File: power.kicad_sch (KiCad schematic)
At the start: 47 parts, among them J3 Barrel_Jack_Switch, Q10 RJK0355DSP, Q7 DMP3037LSS-13, Q8 2N7002, Q9 RJK0355DSP, U5 MIC2101

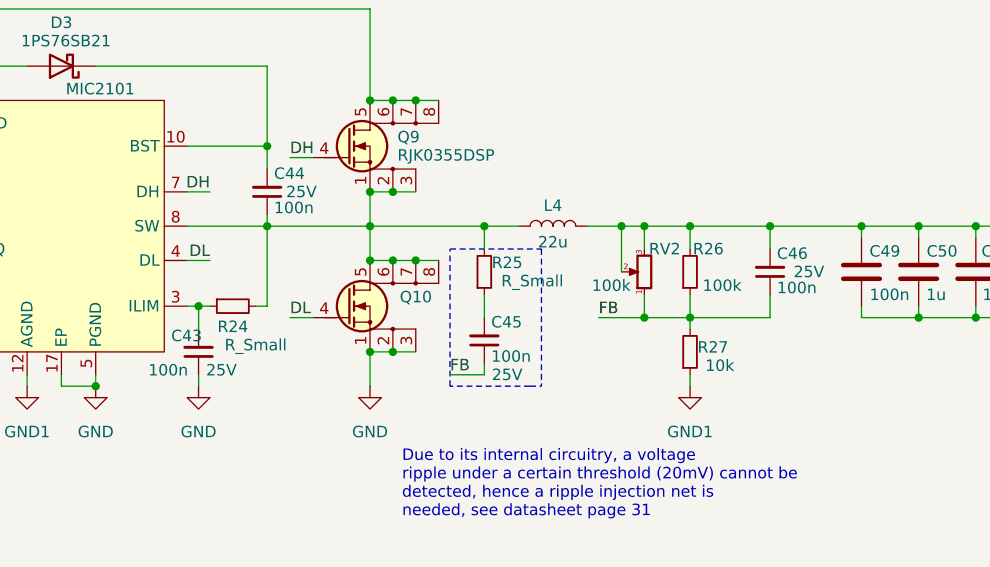
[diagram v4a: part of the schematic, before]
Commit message: small corrections to PCB, fixed some capacitors' voltage ratings and footprints to make BOM more uniform
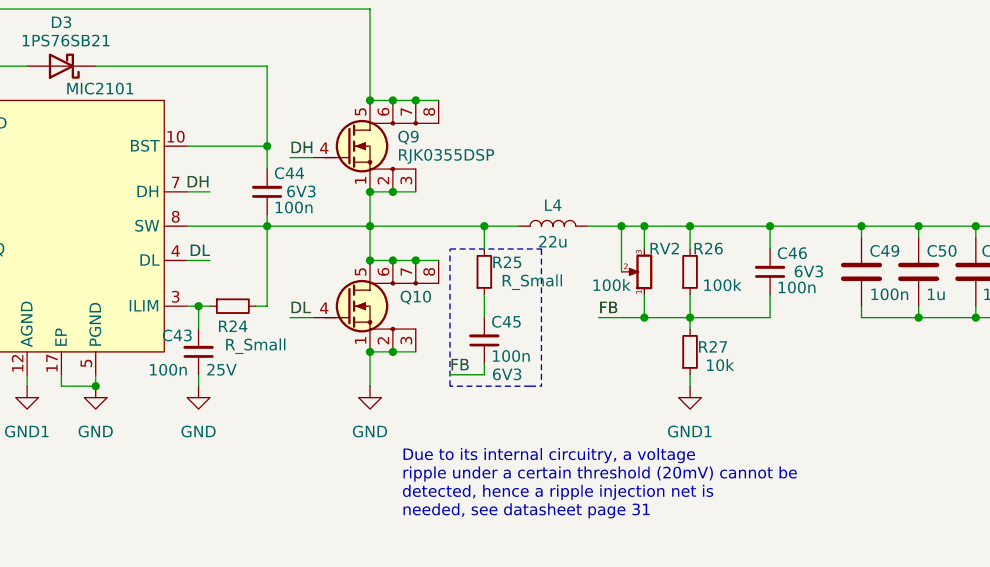
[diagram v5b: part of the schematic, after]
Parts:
- C41, C42: Voltage Rating 25V -> 16V
- C44, C45, C46: footprint Capacitor_SMD:C_0805_2012Metric -> Capacitor_SMD:C_0603_1608Metric; Voltage Rating 25V -> 6V3
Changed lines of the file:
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@@
 			)
 		)
-		(property "Footprint" "Capacitor_SMD:C_0805_2012Metric"
+		(property "Footprint" "Capacitor_SMD:C_0603_1608Metric"
 			(at 146.05 50.8 0)
 			(effects
@@
 			)
 		)
-		(property "Voltage Rating" "25V"
+		(property "Voltage Rating" "6V3"
 			(at 149.86 50.8 0)
 			(effects
@@
 			)
 		)
-		(property "Voltage Rating" "25V"
+		(property "Voltage Rating" "16V"
 			(at 104.14 39.37 0)
 			(effects
@@
 			)
 		)
-		(property "Voltage Rating" "25V"
+		(property "Voltage Rating" "16V"
 			(at 104.14 46.99 0)
 			(effects
@@
 			)
 		)
-		(property "Footprint" "Capacitor_SMD:C_0805_2012Metric"
+		(property "Footprint" "Capacitor_SMD:C_0603_1608Metric"
 			(at 170.18 67.31 0)
 			(effects
@@
 			)
 		)
-		(property "Voltage Rating" "25V"
+		(property "Voltage Rating" "6V3"
 			(at 172.72 71.12 0)
 			(effects
@@
 			)
 		)
+		(property "Store Link" ""
+			(at 170.18 67.31 0)
+			(effects
+				(font
+					(size 1.27 1.27)
+				)
+				(hide yes)
+			)
+		)
+		(property "Dielectric (capacitors)" ""
+			(at 170.18 67.31 0)
+			(effects
+				(font
+					(size 1.27 1.27)
+				)
+				(hide yes)
+			)
+		)
+		(property "PN" ""
+			(at 170.18 67.31 0)
+			(effects
+				(font
+					(size 1.27 1.27)
+				)
+				(hide yes)
+			)
+		)
 		(pin "1"
 		)
@@
 			)
 		)
-		(property "Footprint" "Capacitor_SMD:C_0805_2012Metric"
+		(property "Footprint" "Capacitor_SMD:C_0603_1608Metric"
 			(at 201.93 59.69 0)
 			(effects
@@
 			)
 		)
-		(property "Voltage Rating" "25V"
+		(property "Voltage Rating" "6V3"
 			(at 206.248 59.69 0)
 			(effects
@@
 			)
 		)
+		(property "Store Link" ""
+			(at 201.93 59.69 0)
+			(effects
+				(font
+					(size 1.27 1.27)
+				)
+				(hide yes)
+			)
+		)
+		(property "Dielectric (capacitors)" ""
+			(at 201.93 59.69 0)
+			(effects
+				(font
+					(size 1.27 1.27)
+				)
+				(hide yes)
+			)
+		)
+		(property "PN" ""
+			(at 201.93 59.69 0)
+			(effects
+				(font
+					(size 1.27 1.27)
+				)
+				(hide yes)
+			)
+		)
 		(pin "1"
 		)
@@
 		(dnp no)
 		(property "Reference" "C43"
-			(at 135.382 66.802 0)
+			(at 134.366 66.802 0)
 			(effects
 				(font

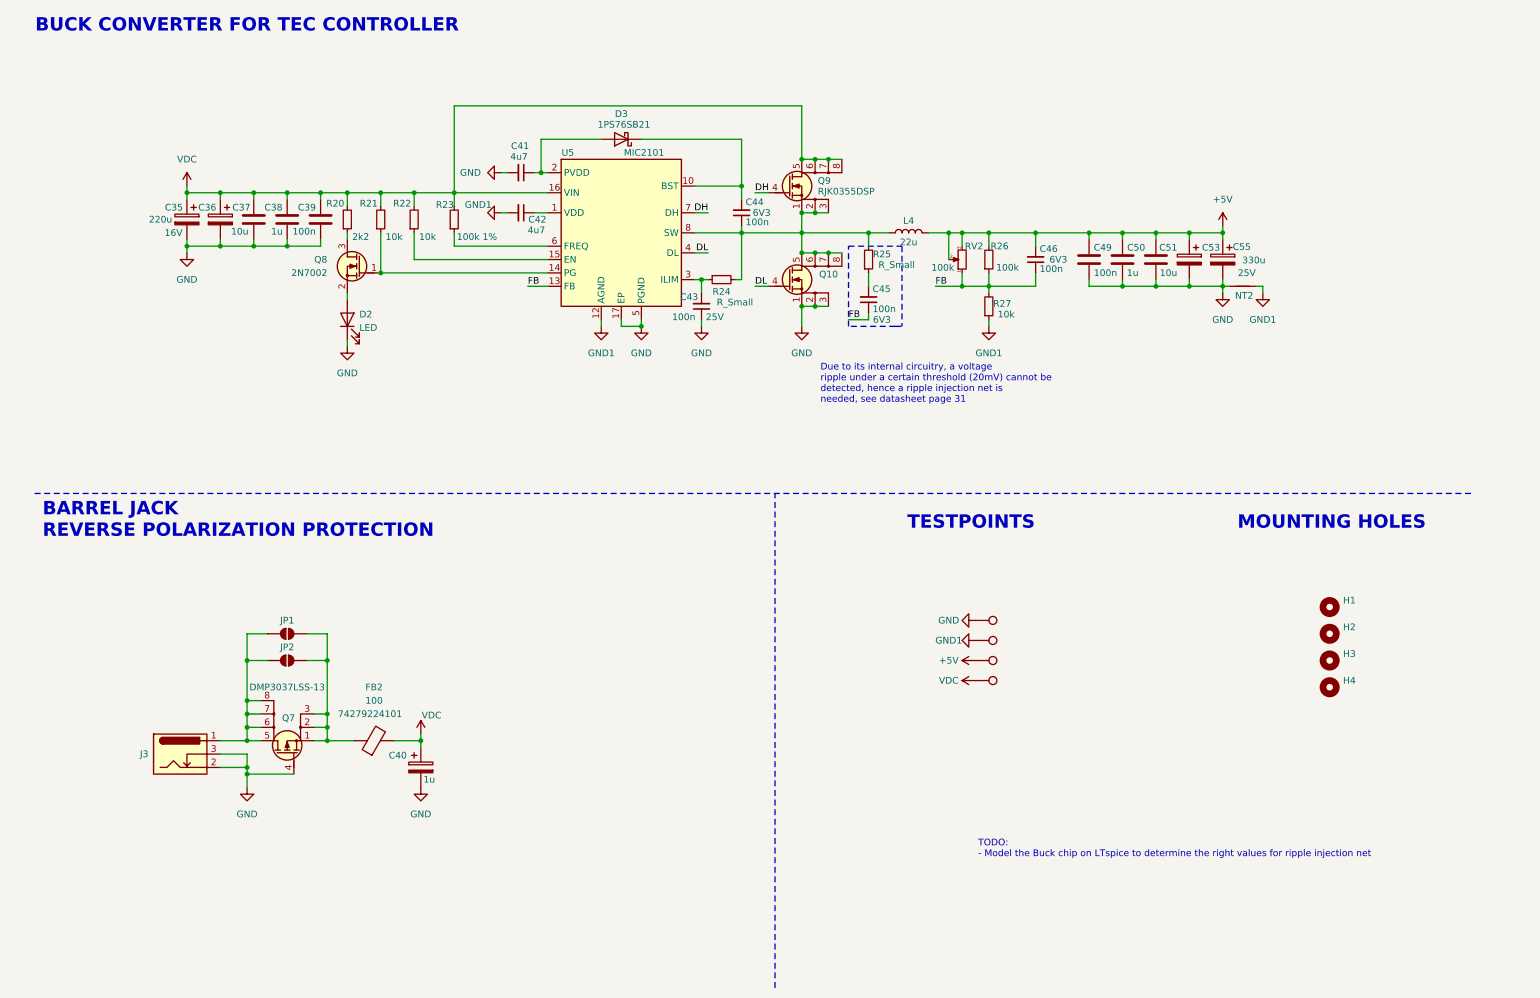
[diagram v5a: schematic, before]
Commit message: feat: made possible to swap butterfly pins for compatibility
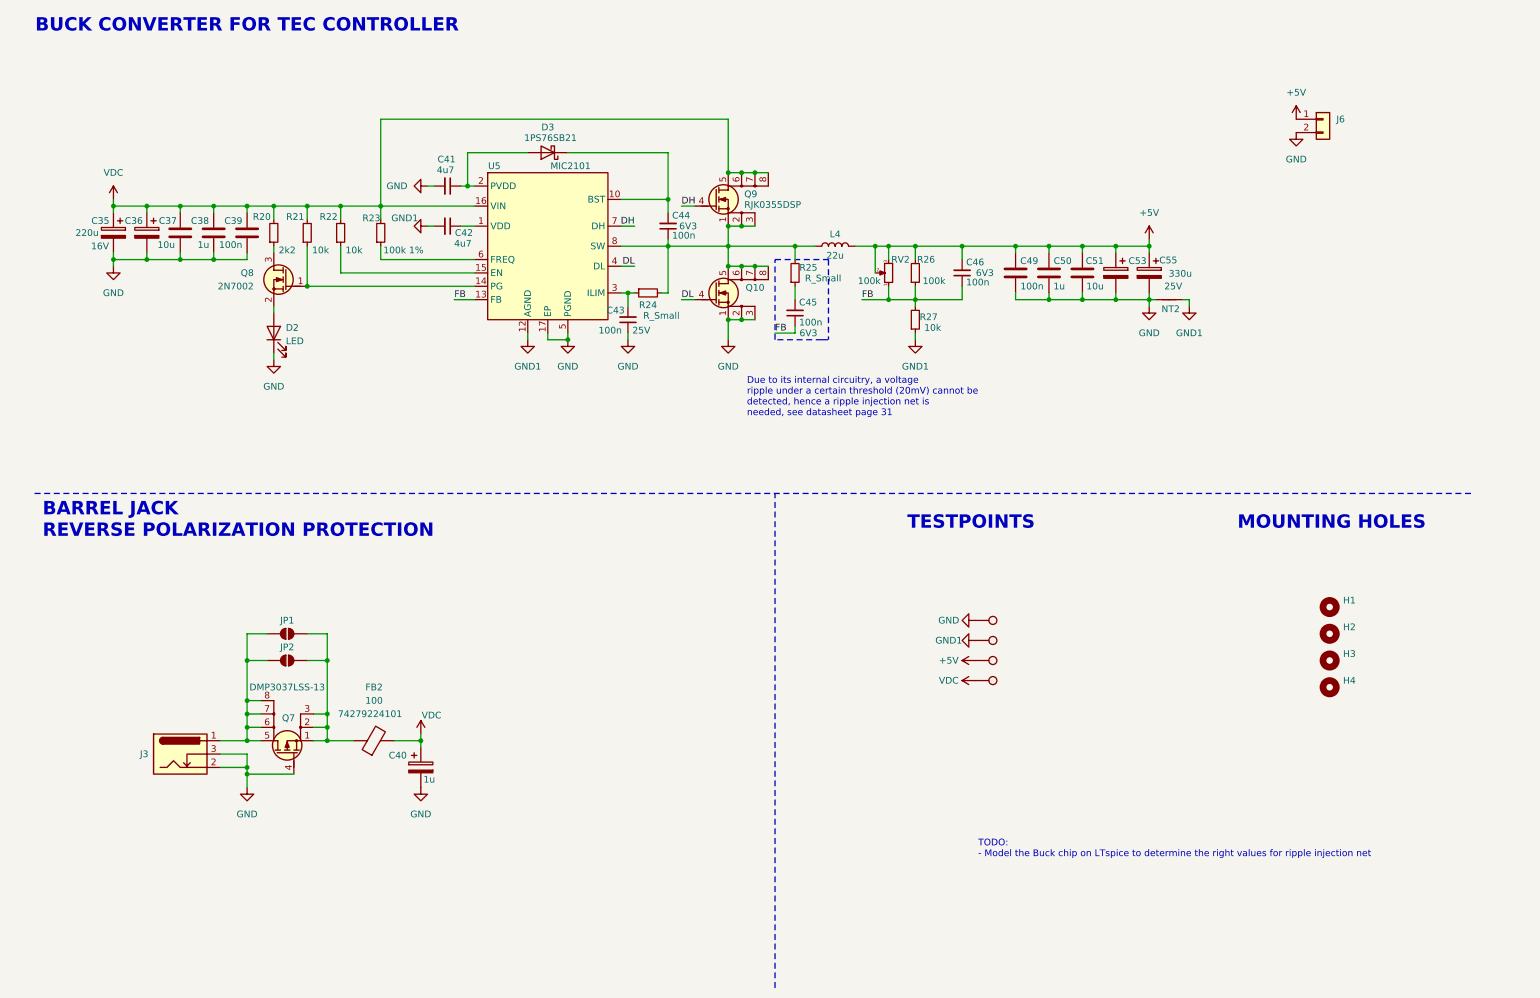
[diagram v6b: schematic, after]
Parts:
- added J6: Conn_01x02, Connector_JST:JST_XH_B2B-XH-AM_1x02_P2.50mm_Vertical, symbol Connector_Generic:Conn_01x02
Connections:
- net +5V: now also J6.1 (Pin_1)
- net GND: now also J6.2 (Pin_2)
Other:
- moved on the sheet: C35, C36, C37, C38, C39, C41, C42, C43, C44, C45, C46, C49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

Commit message: fix: small corrections to the pcb, added PNs and store link to mouser for each component
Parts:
- C35, C36: PN (none) -> EDK227M025A9MAA; Store Link (none) -> https://www.mouser.it/ProductDetail/KEMET/EDK227M025A9MAA?q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
- C37, C51: PN (none) -> TMK212BBJ106MG-T; Store Link (none) -> https://www.mouser.it/ProductDetail/TAIYO-YUDEN/TMK212BBJ10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
- C38, C50: PN (none) -> 885012207078; Store Link (none) -> https://www.mouser.it/ProductDetail/Wurth-Elektronik/885012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
- C39, C43, C49: PN (none) -> CL21F104ZBANNNC; Store Link (none) -> https://www.mouser.it/ProductDetail/Samsung-Electro-Mechani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
- C40: PN EEV337M025S9MAA -> EDH105M050A9BAA; Store Link (none) -> https://www.mouser.it/ProductDetail/KEMET/EDH105M050A9BAA?q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
- C41, C42: PN (none) -> C1608X5R1E475K080AC; Store Link (none) -> https://www.mouser.it/ProductDetail/TDK/C1608X5R1E475K080AC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
- C44, C46: PN (none) -> CL10B104KB8NNND; Store Link (none) -> https://www.mouser.it/ProductDetail/Samsung-Electro-Mechani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
- C45: PN (none) -> CL10B104KB8NNND; Store Link (none) -> https://www.mouser.it/ProductDetail/Samsung-Electro-Mechani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; now left out of the parts list
- C53, C55: Store Link (none) -> https://www.mouser.it/ProductDetail/KEMET/EEV337M025S9MAA?q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
- D2, R24, R25, TP12, TP13, TP14, TP15: now left out of the parts list
- D3: value 1PS76SB21 -> BAT54; PN (none) -> BAT54; Store Link (none) -> https://www.mouser.it/ProductDetail/Diotec-Semiconductor/BA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; Voltage Rating (none) -> 30V
- J6: value Conn_01x02 -> 5V EXT; now left out of the parts list
- L4: Store Link (none) -> https://www.mouser.it/ProductDetail/TAIYO-YUDEN/NRS8040T220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
- Q10, Q9: PN (none) -> RJK0355DSP; Store Link (none) -> https://www.mouser.it/ProductDetail/Renesas-Electronics/RJK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
- Q8: PN (none) -> 2N7002; Store Link (none) -> https://www.mouser.it/ProductDetail/Diotec-Semiconductor/2N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
- R20: PN (none) -> CRCW06032K20FKEA; Store Link (none) -> https://www.mouser.it/ProductDetail/Vishay-Dale/CRCW06032K2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
- R21, R22: PN (none) -> CRCW060310K0FKEC; Store Link (none) -> https://www.mouser.it/ProductDetail/Vishay-Dale/CRCW060310K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
- R23: PN (none) -> RC0603FR-10100KL; Store Link (none) -> https://www.mouser.it/ProductDetail/YAGEO/RC0603FR-10100KL?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
- R26: value 100k -> 5k6; PN (none) -> CRCW06035K60FKEA; Store Link (none) -> https://www.mouser.it/ProductDetail/Vishay-Dale/CRCW06035K6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
- R27: value 10k -> 1k; PN (none) -> RC0603FR-7W1KL; Store Link (none) -> https://www.mouser.it/ProductDetail/YAGEO/RC0603FR-7W1KL?qs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
- RV2: value 100k -> 10k; footprint PCM_Potentiometer_SMD_AKL:Potentiometer_Bourns_3214W_Vertical -> PCM_Potentiometer_SMD_AKL:Potentiometer_Bourns_3224X_Vertical; PN (none) -> 3224X-1-103E; Store Link (none) -> https://www.mouser.it/ProductDetail/Bourns/3224X-1-103E?qs=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
- U5: PN (none) -> MIC2101YML-TR; Store Link (none) -> https://www.mouser.it/ProductDetail/Microchip-Technology/MI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

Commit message: fix: shorted PVDD and VDD on MIC
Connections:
- net at C41.1, D3.2 (A), U5.2 (PVDD): now also C42.1, U5.1 (VDD)
